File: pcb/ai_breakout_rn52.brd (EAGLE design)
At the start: 35.6 x 51.3 mm, 8 parts, among them IC1 RN-52, J1 1X20, J2 1X20

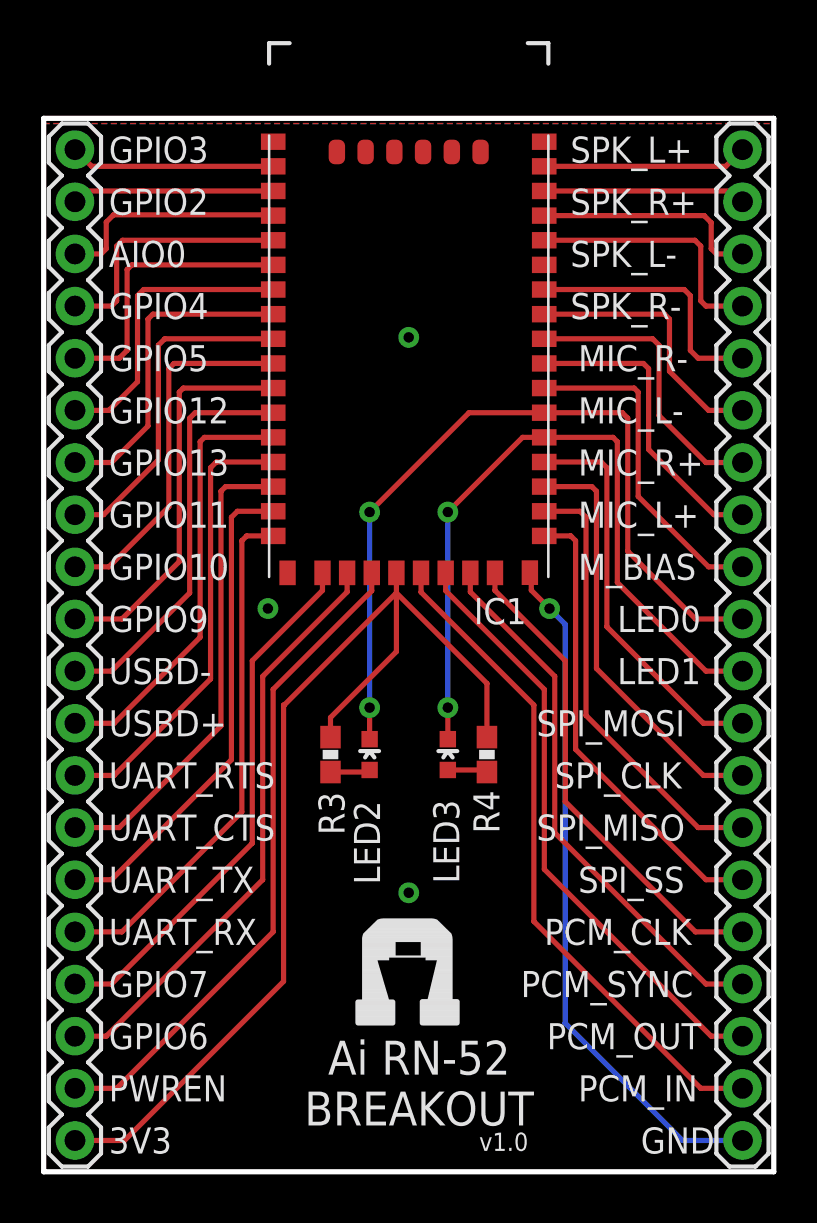
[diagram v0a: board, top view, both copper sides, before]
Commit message: added BOM
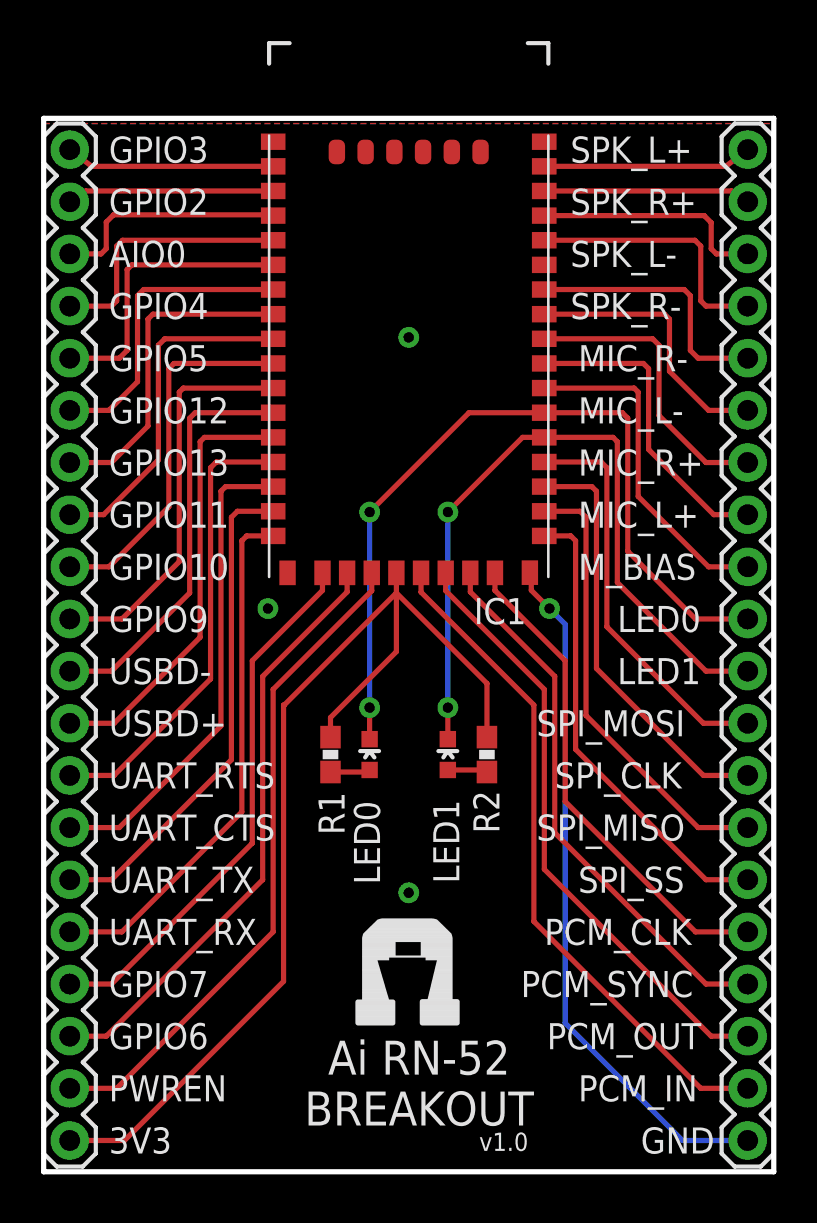
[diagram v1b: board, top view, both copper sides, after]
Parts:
- removed LED2, LED3: (no value), Ai_LED:0603-LED
- removed R3, R4: (no value), Ai_Passives:0603-RES
- added LED0: YELLOW, Ai_LED:LED-0603
- added LED1: BLUE, Ai_LED:LED-0603
- added R1: 300, Ai_Passives:RES-0603
- added R2: 1K, Ai_Passives:RES-0603
- moved J1 0.25 mm to (1.27, 25.7)
- moved J2 0.25 mm to (34.3, 25.7)
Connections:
- net 3V3: now also R1.1, R2.1; no longer R3.1, R4.1
- net LED0: now also LED0.C; no longer LED2.C
- net LED1: now also LED1.C; no longer LED3.C
- net N$6: now also LED0.A, R1.2; no longer LED2.A, R3.2
- net N$7: now also LED1.A, R2.2; no longer LED3.A, R4.2

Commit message: New breaboardable version.
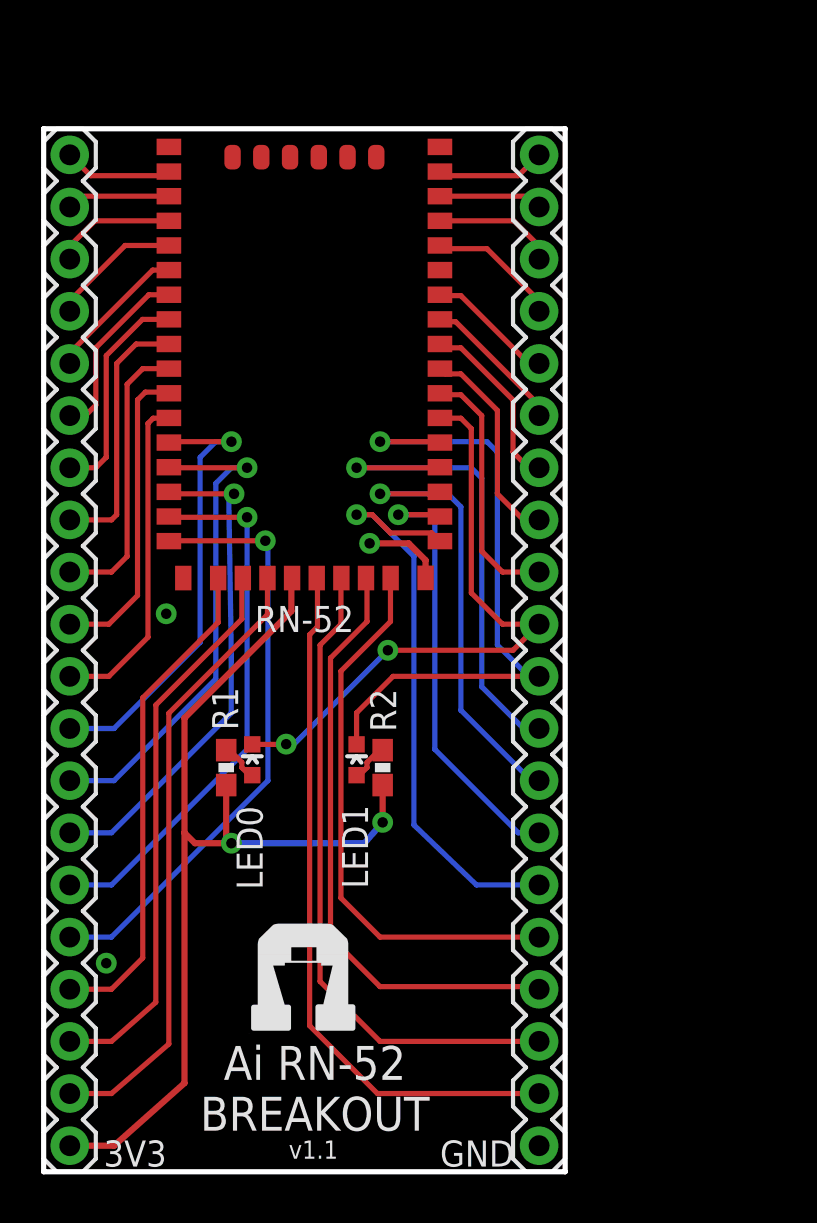
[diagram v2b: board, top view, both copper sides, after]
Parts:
- removed IC1: RN-52, Ai_IC:RN-52
- added RN-52: RN-52, Ai_IC:RN-52
- moved J2 10.2 mm to (24.1, 25.4)
- moved LED0 5.72 mm to (10.2, 20.1)
- moved R1 5.12 mm to (8.89, 19.7), turned to 90 degrees
- moved R2 5.12 mm to (16.5, 19.7), turned to 90 degrees
- moved U$3 5.09 mm to (12.7, 9.02)
- moved LED1 4.45 mm to (15.2, 20.1)
- moved J1 0.25 mm to (1.27, 25.4)
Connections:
- net 3V3: now also RN-52.22; no longer IC1.22
- net AICO0: now also RN-52.4; no longer IC1.4
- net GND: now also RN-52.1, RN-52.18, RN-52.27, RN-52.39, RN-52.44, RN-52.45, RN-52.46, RN-52.47, RN-52.48, RN-52.49, RN-52.50; no longer IC1.1, IC1.18, IC1.27, IC1.39, IC1.44, IC1.45, IC1.46, IC1.47, IC1.48, IC1.49, IC1.50
- net GPIO10: now also RN-52.10; no longer IC1.10
- net GPIO11: now also RN-52.9; no longer IC1.9
- net GPIO12: now also RN-52.7; no longer IC1.7
- net GPIO13: now also RN-52.8; no longer IC1.8
- net GPIO2: now also RN-52.3; no longer IC1.3
- net GPIO3: now also RN-52.2; no longer IC1.2
- net GPIO4: now also RN-52.5; no longer IC1.5
- net GPIO5: now also RN-52.6; no longer IC1.6
- net GPIO6: now also RN-52.20; no longer IC1.20
- net GPIO7: now also RN-52.19; no longer IC1.19
- net GPIO9: now also RN-52.11; no longer IC1.11
- net LED0: now also RN-52.33; no longer IC1.33
- net LED1: now also RN-52.32; no longer IC1.32
- net MIC_BIAS: now also RN-52.34; no longer IC1.34
- net MIC_L+: now also RN-52.35; no longer IC1.35
- net MIC_L-: now also RN-52.37; no longer IC1.37
- net MIC_R+: now also RN-52.36; no longer IC1.36
- net MIC_R-: now also RN-52.38; no longer IC1.38
- net PCM_CLK: now also RN-52.26; no longer IC1.26
- net PCM_IN: now also RN-52.23; no longer IC1.23
- net PCM_OUT: now also RN-52.24; no longer IC1.24
- net PCM_SYNC: now also RN-52.25; no longer IC1.25
- net PWREN: now also RN-52.21; no longer IC1.21
- net SPI_CLK: now also RN-52.30; no longer IC1.30
- net SPI_MISO: now also RN-52.29; no longer IC1.29
- net SPI_MOSI: now also RN-52.31; no longer IC1.31
- net SPI_SS: now also RN-52.28; no longer IC1.28
- net SPKR_L+: now also RN-52.43; no longer IC1.43
- net SPKR_L-: now also RN-52.41; no longer IC1.41
- net SPKR_R+: now also RN-52.42; no longer IC1.42
- net SPKR_R-: now also RN-52.40; no longer IC1.40
- net UART_CTS: now also RN-52.15; no longer IC1.15
- net UART_RTS: now also RN-52.14; no longer IC1.14
- net UART_RX: now also RN-52.17; no longer IC1.17
- net UART_TX: now also RN-52.16; no longer IC1.16
- net USBD+: now also RN-52.13; no longer IC1.13
- net USBD-: now also RN-52.12; no longer IC1.12
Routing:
- net GND: track 33.8 -> 3.93 mm, vias 4 -> 3
- net LED0: track 39.4 -> 30.1 mm
- net GPIO5: track 14.1 -> 7.01 mm
- net MIC_R-: track 12.9 -> 6.22 mm
- net SPKR_R-: track 12.8 -> 6.46 mm
- net GPIO4: track 12.8 -> 6.46 mm
- net MIC_L-: track 13.3 -> 7.07 mm
- net GPIO12: track 14.8 -> 8.90 mm
- net SPI_SS: track 22.8 -> 28.6 mm, vias 0 -> 1
- net MIC_R+: track 14.4 -> 8.81 mm
- net AICO0: track 11.5 -> 5.97 mm
- net SPKR_L-: track 11.4 -> 5.97 mm
- net GPIO13: track 16.0 -> 10.7 mm
- net SPKR_R+: track 10.1 -> 5.05 mm
- net GPIO2: track 10.1 -> 5.05 mm
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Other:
- board size 35.6 x 51.3 mm -> 25.4 x 50.8 mm
- board text added: "MIC_BIAS"
- board text added: "http://acrobotic.com/rn-52"
- board text added: "v1.1"
- board text removed: "AIO0"
- board text removed: "M_BIAS"
- board text removed: "http://acrobotic.com/breakout/rn-52"
- board text removed: "v1.0"

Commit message: updating
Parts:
- added FRAME1: FRAME-LETTER, Ai_Miscellany:CREATIVE-COMMONS
- RN-52: value RN-52 -> RN52; device Ai_IC:RN-52 -> Ai_RF:RN52
- U$3: value AI-LOGOL -> AI-LOGOXS; device Ai_Miscellany:AI-LOGO-L -> Ai_Miscellany:AI-LOGO-XS
- moved U$3 2.17 mm to (12.4, 11.2)
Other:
- board text added: "@MakerBro"
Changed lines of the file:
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@@
 <?xml version="1.0" encoding="utf-8"?>
 <!DOCTYPE eagle SYSTEM "eagle.dtd">
-<eagle version="6.5.0">
+<eagle version="7.1.0">
 <drawing>
 <settings>
@@
 <layer number="49" name="Reference" color="7" fill="1" visible="no" active="yes"/>
 <layer number="50" name="dxf" color="7" fill="1" visible="no" active="no"/>
-<layer number="51" name="tDocu" color="7" fill="1" visible="no" active="yes"/>
-<layer number="52" name="bDocu" color="7" fill="1" visible="no" active="yes"/>
+<layer number="51" name="tDocu" color="7" fill="1" visible="yes" active="yes"/>
+<layer number="52" name="bDocu" color="7" fill="1" visible="yes" active="yes"/>
 <layer number="53" name="tGND_GNDA" color="7" fill="9" visible="no" active="no"/>
 <layer number="54" name="bGND_GNDA" color="1" fill="9" visible="no" active="no"/>
 <layer number="56" name="wert" color="7" fill="1" visible="no" active="no"/>
 <layer number="57" name="tCAD" color="7" fill="1" visible="no" active="no"/>
+<layer number="59" name="tCarbon" color="7" fill="1" visible="no" active="no"/>
+<layer number="60" name="bCarbon" color="7" fill="1" visible="no" active="no"/>
+<layer number="90" name="Modules" color="5" fill="1" visible="no" active="no"/>
 <layer number="91" name="Nets" color="2" fill="1" visible="no" active="no"/>
 <layer number="92" name="Busses" color="1" fill="1" visible="no" active="no"/>
@@
 <layer number="97" name="Info" color="7" fill="1" visible="no" active="no"/>
 <layer number="98" name="Guide" color="6" fill="1" visible="no" active="no"/>
+<layer number="99" name="SpiceOrder" color="7" fill="1" visible="no" active="no"/>
 <layer number="100" name="Muster" color="7" fill="1" visible="no" active="no"/>
 <layer number="101" name="Patch_Top" color="12" fill="4" visible="yes" active="yes"/>
@@
 <layer number="112" name="tSilk" color="7" fill="1" visible="yes" active="yes"/>
 <layer number="113" name="Route13" color="7" fill="1" visible="no" active="no"/>
+<layer number="114" name="Badge_Outline" color="7" fill="1" visible="yes" active="yes"/>
+<layer number="115" name="ReferenceISLANDS" color="7" fill="1" visible="yes" active="yes"/>
 <layer number="116" name="Patch_BOT" color="9" fill="4" visible="yes" active="yes"/>
 <layer number="117" name="mPads" color="7" fill="1" visible="no" active="no"/>
@@
 <layer number="223" name="223bmp" color="24" fill="1" visible="no" active="no"/>
 <layer number="224" name="224bmp" color="25" fill="1" visible="no" active="no"/>
+<layer number="225" name="225bmp" color="7" fill="1" visible="yes" active="yes"/>
+<layer number="226" name="226bmp" color="7" fill="1" visible="yes" active="yes"/>
+<layer number="227" name="227bmp" color="7" fill="1" visible="yes" active="yes"/>
+<layer number="228" name="228bmp" color="7" fill="1" visible="yes" active="yes"/>
+<layer number="229" name="229bmp" color="7" fill="1" visible="yes" active="yes"/>
+<layer number="230" name="230bmp" color="7" fill="1" visible="yes" active="yes"/>
+<layer number="231" name="231bmp" color="7" fill="1" visible="yes" active="yes"/>
 <layer number="248" name="Housing" color="7" fill="1" visible="yes" active="yes"/>
 <layer number="249" name="Edge" color="7" fill="1" visible="yes" active="yes"/>
@@
 <layer number="251" name="SMDround" color="7" fill="1" visible="no" active="no"/>
 <layer number="254" name="cooling" color="7" fill="1" visible="yes" active="yes"/>
+<layer number="255" name="routoute" color="7" fill="1" visible="yes" active="yes"/>
 </layers>
 <board>
@@
 <text x="22.86" y="0.889" size="1.27" layer="22" font="vector" ratio="15" rot="MR0">GND</text>
 <text x="19.304" y="0.254" size="1.27" layer="21" font="vector" ratio="15">GND</text>
+<text x="7.62" y="-17.78" size="1.778" layer="51">@MakerBro</text>
 </plain>
 <attributes>
@@
 <pass name="Default">
 <param name="RoutingGrid" value="50mil"/>
+<param name="AutoGrid" value="1"/>
+<param name="Efforts" value="0"/>
+<param name="TopRouterVariant" value="1"/>
 <param name="tpViaShape" value="round"/>
 <param name="PrefDir.1" value="|"/>
@@
 <element name="J2" library="Ai_Connectors" package="1X20" value="1X20" x="24.13" y="25.4" smashed="yes" rot="R90"/>
 <element name="J1" library="Ai_Connectors" package="1X20" value="1X20" x="1.27" y="25.4" smashed="yes" rot="R270"/>
-<element name="RN-52" library="Ai_IC" package="RN-52" value="RN-52" x="12.7" y="40.386" smashed="yes">
+<element name="RN-52" library="Ai_RF" package="RN52" value="RN52" x="12.7" y="40.386" smashed="yes">
 <attribute name="NAME" x="10.287" y="26.289" size="1.27" layer="25" font="vector" ratio="15"/>
 </element>
-<element name="U$3" library="Ai_Miscellany" package="AI-LOGO-L" value="AI-LOGOL" x="12.7" y="9.017"/>
+<element name="U$3" library="Ai_Miscellany" package="AI-LOGO-XS" value="AI-LOGOXS" x="12.446" y="11.176"/>
+<element name="FRAME1" library="Ai_Miscellany" package="CREATIVE-COMMONS" value="FRAME-LETTER" x="13.97" y="-1.27">
+<attribute name="REV" value="1.1" x="13.97" y="-1.27" size="1.778" layer="27" display="off"/>
+</element>
 </elements>
 <signals>
@@
 <wire x1="9.652" y1="19.685" x2="9.652" y2="19.939" width="0.254" layer="1"/>
 <wire x1="9.652" y1="19.939" x2="9.056" y2="20.535" width="0.254" layer="1"/>
-<wire x1="9.056" y1="20.535" x2="8.89" y2="20.535" width="0.254" layer="1"/>
+<wire x1="9.056" y1="20.535" x2="8.89" y2="20.585" width="0.254" layer="1"/>
 </signal>
 <signal name="N$7">
@@
 <wire x1="15.748" y1="19.685" x2="15.748" y2="19.939" width="0.254" layer="1"/>
 <wire x1="15.748" y1="19.939" x2="16.344" y2="20.535" width="0.254" layer="1"/>
-<wire x1="16.344" y1="20.535" x2="16.51" y2="20.535" width="0.254" layer="1"/>
+<wire x1="16.344" y1="20.535" x2="16.51" y2="20.585" width="0.254" layer="1"/>
 </signal>
 <signal name="LED0">
@@
 <wire x1="15.621" y1="16.002" x2="16.51" y2="17.018" width="0.3048" layer="16"/>
 <via x="16.51" y="17.018" extent="1-16" drill="0.508"/>
-<wire x1="16.51" y1="17.018" x2="16.51" y2="18.835" width="0.3048" layer="1"/>
+<wire x1="16.51" y1="17.018" x2="16.51" y2="18.785" width="0.3048" layer="1"/>
 <wire x1="12.065" y1="27.305" x2="6.858" y2="22.098" width="0.3048" layer="1"/>
 <wire x1="6.858" y1="22.098" x2="6.858" y2="16.51" width="0.3048" layer="1"/>
 <wire x1="6.858" y1="16.51" x2="7.366" y2="16.002" width="0.3048" layer="1"/>
 <wire x1="7.366" y1="16.002" x2="9.144" y2="16.002" width="0.3048" layer="1"/>
-<wire x1="8.89" y1="18.835" x2="8.89" y2="16.383" width="0.3048" layer="1"/>
+<wire x1="8.89" y1="18.785" x2="8.89" y2="16.383" width="0.3048" layer="1"/>
 <wire x1="8.89" y1="16.383" x2="9.144" y2="16.129" width="0.3048" layer="1"/>
 <wire x1="9.144" y1="16.129" x2="9.144" y2="16.002" width="0.3048" layer="1"/>
